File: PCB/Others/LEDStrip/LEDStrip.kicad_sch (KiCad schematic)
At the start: 14 parts

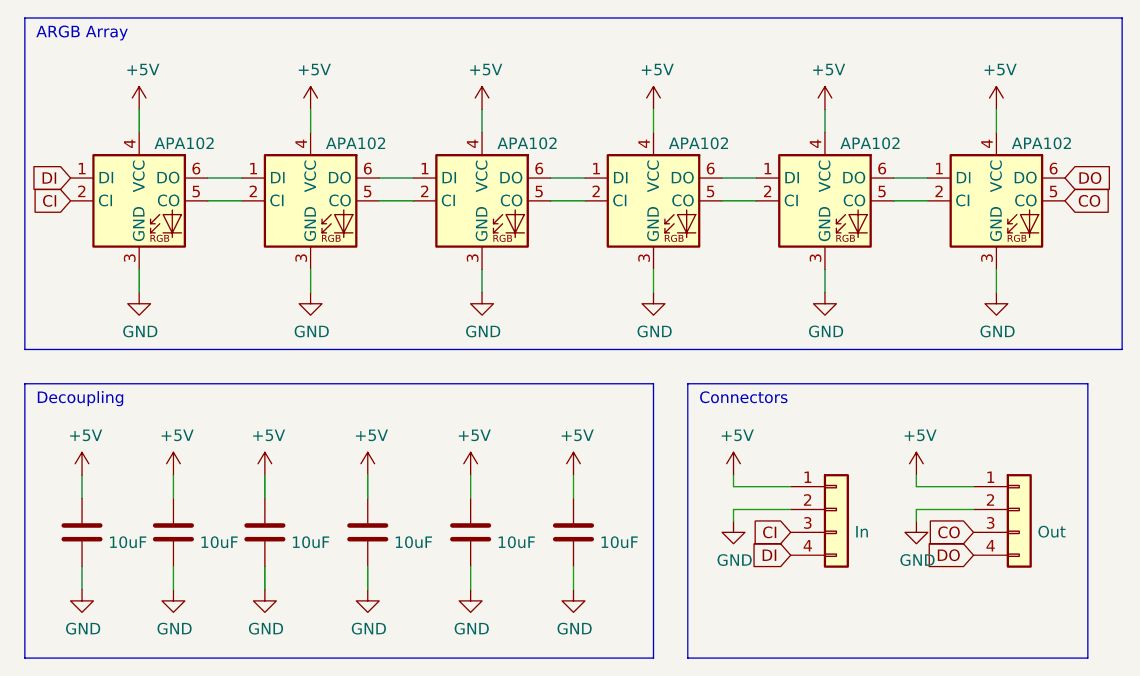
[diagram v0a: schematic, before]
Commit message: Upgrade KiCad files from 6.0 to 7.0.
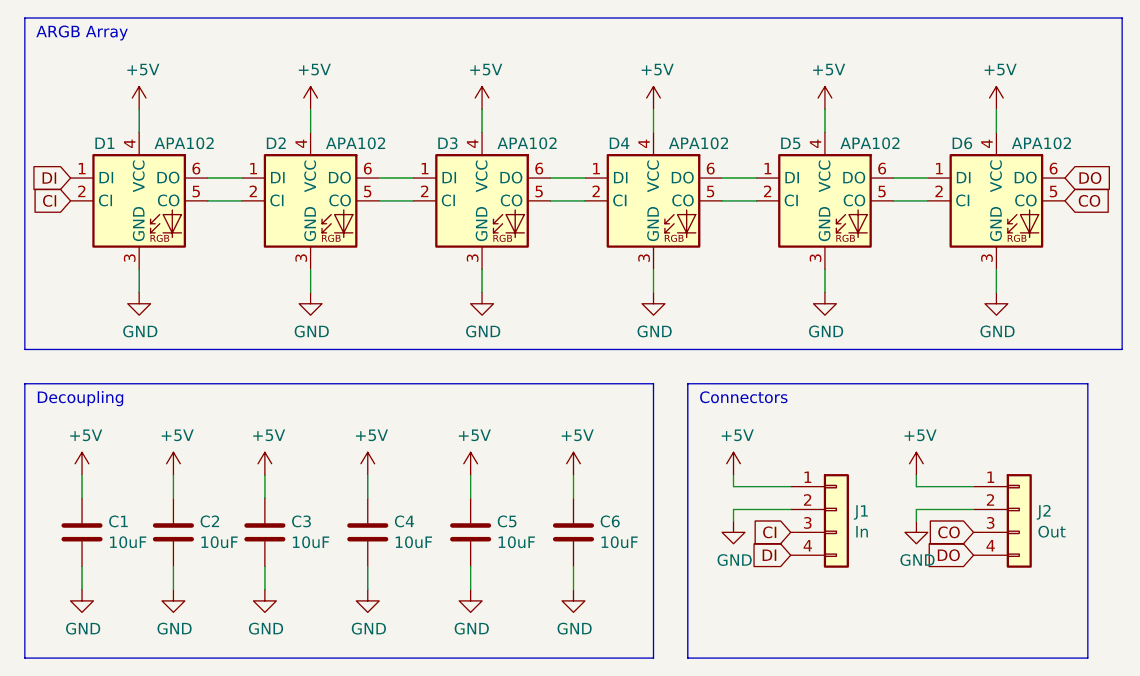
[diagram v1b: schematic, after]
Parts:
- gave numbers to parts that had none: 14
